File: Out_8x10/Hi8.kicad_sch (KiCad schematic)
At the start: 58 parts, among them J5 Conn_01x09, J6 Conn_01x10, Q1 2N7002, Q10 AO3401A, Q11 AO3401A, Q12 AO3401A, Q13 2N7002, Q14 2N7002, Q15 AO3401A, Q16 AO3401A, Q2 2N7002, Q3 2N7002, Q4 AO3401A, Q5 AO3401A, Q6 AO3401A, Q7 2N7002, Q8 2N7002, Q9 2N7002, U10 L78L24_SOT89, U11 L78L24_SOT89, U12 L78L24_SOT89, U13 L78L24_SOT89, U6 L78L24_SOT89, U7 L78L24_SOT89, U8 L78L24_SOT89, U9 L78L24_SOT89

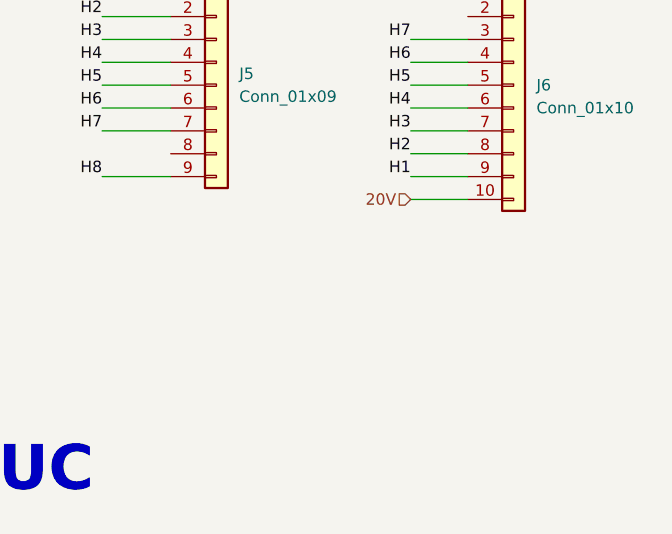
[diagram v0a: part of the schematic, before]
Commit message: updated layout
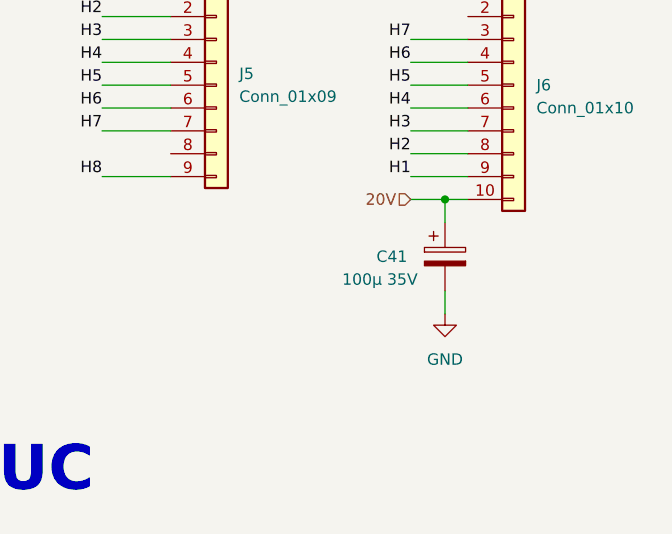
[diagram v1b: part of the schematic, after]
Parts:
- added C41: 100µ 35V, Capacitor_SMD:CP_Elec_6.3x7.7, symbol Device:C_Polarized
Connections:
- net 20V: now also C41.1
- net GND: now also C41.2
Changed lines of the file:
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@@
     (title "High Side Switches")
     (date "2023-10-08")
-    (rev "00.10")
+    (rev "0.10")
   )
   (junction (at 173.99 132.08) (diameter 0) (color 0 0 0 0)
@@
   (junction (at 82.55 132.08) (diameter 0) (color 0 0 0 0)
   )
+  (junction (at 256.54 144.78) (diameter 0) (color 0 0 0 0)
+  )
   (junction (at 158.75 25.4) (diameter 0) (color 0 0 0 0)
   )
@@
     (stroke (width 0) (type default) (color 0 0 0 0))
   )
+  (wire (pts (xy 256.54 144.78) (xy 256.54 147.32))
+    (stroke (width 0) (type default) (color 0 0 0 0))
+  )
   (wire (pts (xy 68.58 73.66) (xy 78.74 73.66))
     (stroke (width 0) (type default) (color 0 0 0 0))
@@
     (stroke (width 0) (type default) (color 0 0 0 0))
   )
+  (wire (pts (xy 256.54 144.78) (xy 259.08 144.78))
+    (stroke (width 0) (type default) (color 0 0 0 0))
+  )
   (wire (pts (xy 68.58 82.55) (xy 72.39 82.55))
     (stroke (width 0) (type default) (color 0 0 0 0))
@@
     (stroke (width 0) (type default) (color 0 0 0 0))
   )
-  (wire (pts (xy 252.73 144.78) (xy 259.08 144.78))
+  (wire (pts (xy 252.73 144.78) (xy 256.54 144.78))
     (stroke (width 0) (type default) (color 0 0 0 0))
   )
@@
   )
   (wire (pts (xy 67.31 123.19) (xy 77.47 123.19))
+    (stroke (width 0) (type default) (color 0 0 0 0))
+  )
+  (wire (pts (xy 256.54 154.94) (xy 256.54 157.48))
     (stroke (width 0) (type default) (color 0 0 0 0))
   )
@@
     (pin "2")
   )
+  (symbol (lib_id "power:GND") (at 256.54 157.48 0) (unit 1)
+    (in_bom yes) (on_board yes) (fields_autoplaced)
+    (property "Reference" "#PWR01" (id 0) (at 256.54 163.83 0)
+      (effects (font (size 1.27 1.27)) hide)
+    )
+    (property "Value" "GND" (id 1) (at 256.54 162.56 0))
+    (property "Footprint" "" (id 2) (at 256.54 157.48 0)
+      (effects (font (size 1.27 1.27)) hide)
+    )
+    (property "Datasheet" "" (id 3) (at 256.54 157.48 0)
+      (effects (font (size 1.27 1.27)) hide)
+    )
+    (pin "1")
+  )
   (symbol (lib_id "Device:C") (at 34.29 78.74 0) (unit 1)
     (in_bom yes) (on_board yes)
@@
     (pin "1")
   )
+  (symbol (lib_id "Device:C_Polarized") (at 256.54 151.13 0) (unit 1)
+    (in_bom yes) (on_board yes)
+    (property "Reference" "C41" (id 0) (at 248.92 151.13 0)
+      (effects (font (size 1.27 1.27)) (justify left))
+    )
+    (property "Value" "100µ 35V" (id 1) (at 245.11 153.67 0)
+      (effects (font (size 1.27 1.27)) (justify left))
+    )
+    (property "Footprint" "Capacitor_SMD:CP_Elec_6.3x7.7" (id 2) (at 257.5052 154.94 0)
+      (effects (font (size 1.27 1.27)) hide)
+    )
+    (property "Datasheet" "~" (id 3) (at 256.54 151.13 0)
+      (effects (font (size 1.27 1.27)) hide)
+    )
+    (pin "1")
+    (pin "2")
+  )
   (symbol (lib_id "Device:R") (at 74.93 132.08 90) (unit 1)

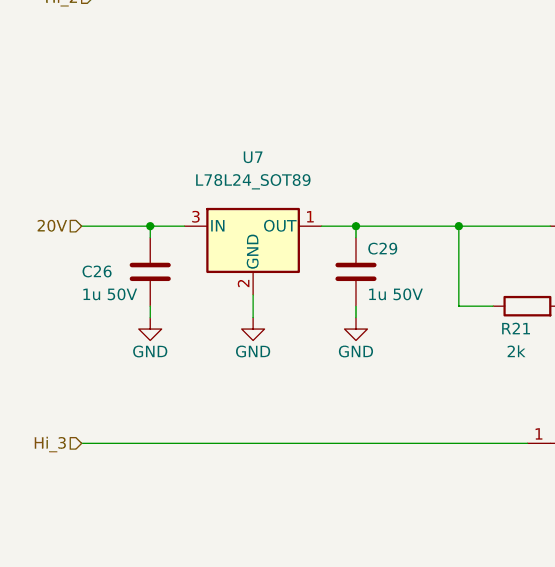
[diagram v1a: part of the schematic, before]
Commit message: updated layout
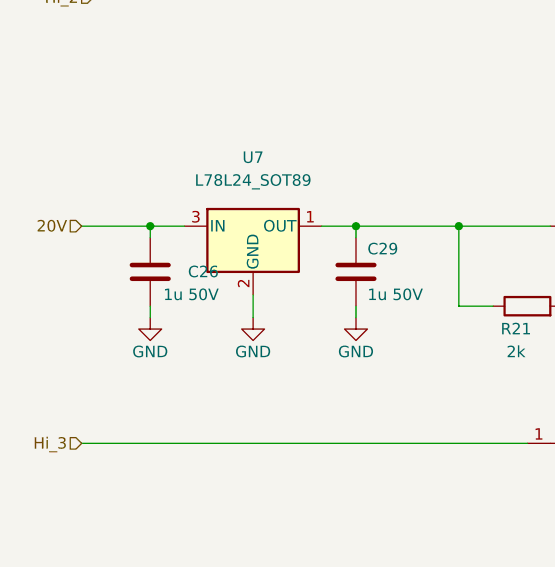
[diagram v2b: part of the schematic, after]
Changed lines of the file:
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@@
     (pin "2")
   )
-  (symbol (lib_id "Device:C") (at 33.02 128.27 0) (unit 1)
+  (symbol (lib_id "Device:C") (at 33.02 128.27 0) (mirror y) (unit 1)
     (in_bom yes) (on_board yes)
-    (property "Reference" "C26" (id 0) (at 25.4 128.27 0)
+    (property "Reference" "C26" (id 0) (at 40.64 128.27 0)
       (effects (font (size 1.27 1.27)) (justify left))
     )
-    (property "Value" "1u 50V" (id 1) (at 25.4 130.81 0)
+    (property "Value" "1u 50V" (id 1) (at 40.64 130.81 0)
       (effects (font (size 1.27 1.27)) (justify left))
     )
-    (property "Footprint" "Capacitor_SMD:C_0603_1608Metric" (id 2) (at 33.9852 132.08 0)
+    (property "Footprint" "Capacitor_SMD:C_0603_1608Metric" (id 2) (at 32.0548 132.08 0)
       (effects (font (size 1.27 1.27)) hide)
     )

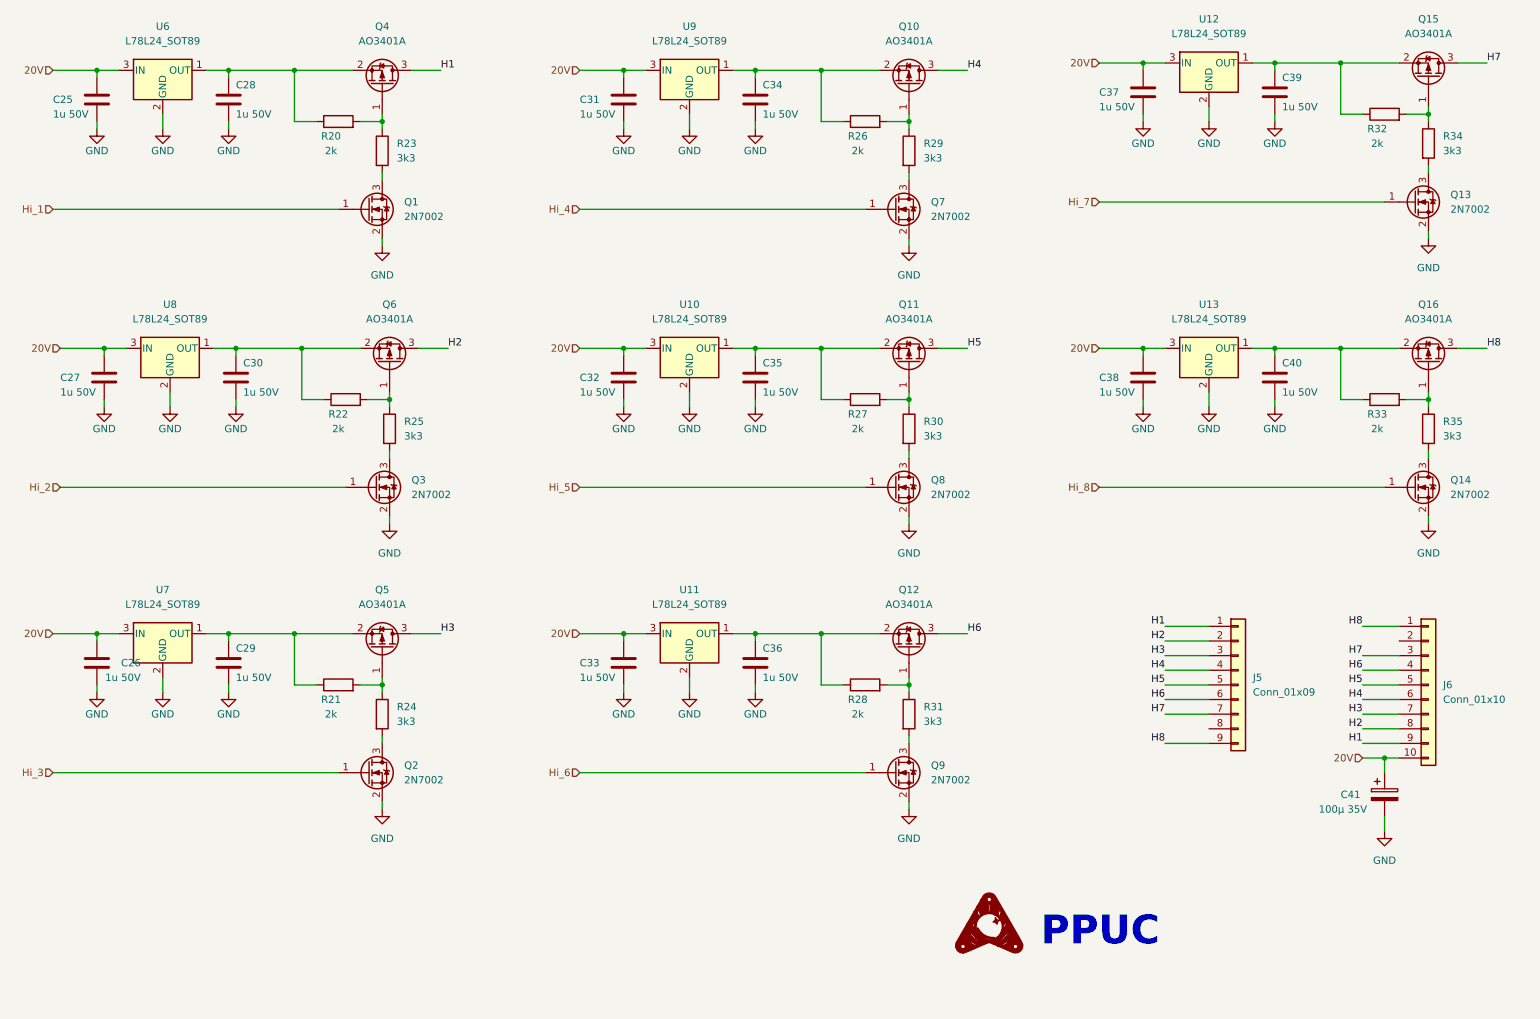
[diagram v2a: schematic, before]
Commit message: updated layout
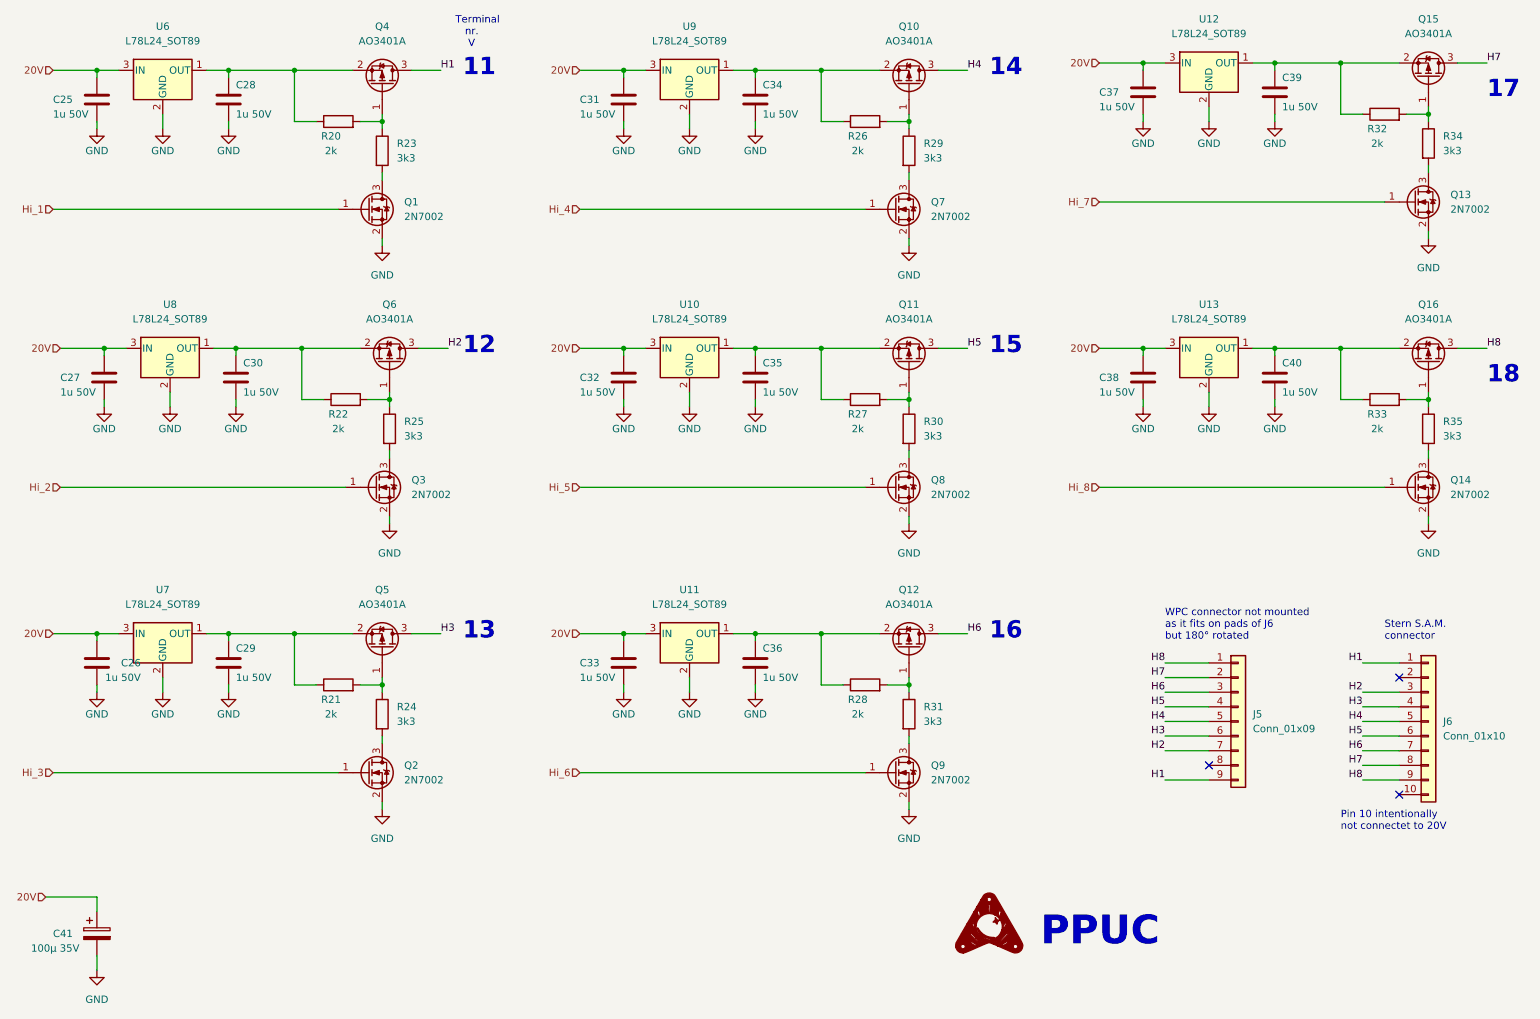
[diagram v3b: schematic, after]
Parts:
- J5: now left out of the parts list
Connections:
- net 20V: no longer J6.10 (Pin_10)
- net H1: now also J5.9 (Pin_9), J6.1 (Pin_1); no longer J5.1 (Pin_1), J6.9 (Pin_9)
- net H2: now also J5.7 (Pin_7), J6.3 (Pin_3); no longer J5.2 (Pin_2), J6.8 (Pin_8)
- net H3: now also J5.6 (Pin_6), J6.4 (Pin_4); no longer J5.3 (Pin_3), J6.7 (Pin_7)
- net H4: now also J5.5 (Pin_5), J6.5 (Pin_5); no longer J5.4 (Pin_4), J6.6 (Pin_6)
- net H5: now also J5.4 (Pin_4), J6.6 (Pin_6); no longer J5.5 (Pin_5), J6.5 (Pin_5)
- net H6: now also J5.3 (Pin_3), J6.7 (Pin_7); no longer J5.6 (Pin_6), J6.4 (Pin_4)
- net H7: now also J5.2 (Pin_2), J6.8 (Pin_8); no longer J5.7 (Pin_7), J6.3 (Pin_3)
- net H8: now also J5.1 (Pin_1), J6.9 (Pin_9); no longer J5.9 (Pin_9), J6.1 (Pin_1)
- no-connect marks 0 -> 3
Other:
- note added: "11"
- note added: "12"
- note added: "13"
- note added: "14"
- note added: "15"
- note added: "16"
- note added: "17"
- note added: "18"
- note added: "Pin 10 intentionally not connectet to 20V"
- note added: "Stern S.A.M. connector"
- note added: "Terminal nr. V"
- note added: "WPC connector not mounted as it fits on pads of J6 but 180° rotated"
- moved on the sheet: C41, J5, J6
